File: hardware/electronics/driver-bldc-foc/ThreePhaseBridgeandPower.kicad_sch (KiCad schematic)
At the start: 1 part, among them U1 DRV8353RS

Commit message: fix pcb 20.7.1635
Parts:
- removed U1: DRV8353RS, symbol Custom:DRV8353RS
- added L1: L_Ferrite_Small, Inductor_SMD:L_Cenker_CKCS8040, symbol Device:L_Ferrite_Small
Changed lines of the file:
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@@
 	(paper "A4")
 	(symbol
-		(lib_id "Custom:DRV8353RS")
-		(at 101.6 90.17 0)
+		(lib_id "Device:L_Ferrite_Small")
+		(at 35.56 35.56 0)
 		(unit 1)
 		(body_style 1)
@@
 		(dnp no)
 		(fields_autoplaced yes)
-		(property "Reference" "U1"
-			(at 101.6 44.45 0)
+		(property "Reference" "L1"
+			(at 38.1 34.2899 0)
 			(show_name no)
 			(do_not_autoplace no)
@@
 					(size 1.27 1.27)
 				)
+				(justify left)
 			)
 		)
-		(property "Value" "DRV8353RS"
-			(at 101.6 46.99 0)
+		(property "Value" "L_Ferrite_Small"
+			(at 38.1 36.8299 0)
 			(show_name no)
 			(do_not_autoplace no)
@@
 					(size 1.27 1.27)
 				)
+				(justify left)
 			)
 		)
-		(property "Footprint" ""
-			(at 21.59 44.45 0)
+		(property "Footprint" "Inductor_SMD:L_Cenker_CKCS8040"
+			(at 35.56 35.56 0)
 			(hide yes)
 			(show_name no)
@@
 		)
 		(property "Datasheet" ""
-			(at 21.59 44.45 0)
+			(at 35.56 35.56 0)
 			(hide yes)
 			(show_name no)
@@
 			)
 		)
-		(property "Description" ""
-			(at 101.6 90.17 0)
+		(property "Description" "Inductor with ferrite core, small symbol"
+			(at 35.56 35.56 0)
 			(hide yes)
 			(show_name no)
@@
 			)
 		)
-		(pin "44"
-		)
-		(pin "27"
-		)
-		(pin "9"
-		)
-		(pin "7"
-		)
-		(pin "32"
-		)
-		(pin "33"
-		)
-		(pin "45"
-		)
-		(pin "30"
-		)
-		(pin "31"
-		)
-		(pin "35"
-		)
-		(pin "29"
-		)
-		(pin "14"
-		)
-		(pin "21"
-		)
-		(pin "16"
-		)
-		(pin "34"
-		)
-		(pin "36"
-		)
-		(pin "49"
-		)
-		(pin "13"
-		)
-		(pin "26"
-		)
-		(pin "47"
-		)
-		(pin "46"
-		)
-		(pin "8"
-		)
-		(pin "28"
-		)
-		(pin "10"
-		)
-		(pin "12"
-		)
-		(pin "23"
-		)
-		(pin "48"
-		)
-		(pin "15"
-		)
-		(pin "22"
-		)
-		(pin "3"
-		)
-		(pin "38"
-		)
-		(pin "37"
-		)
-		(pin "41"
-		)
-		(pin "6"
-		)
-		(pin "17"
-		)
-		(pin "5"
-		)
-		(pin "24"
+		(pin "1"
 		)
 		(pin "2"
-		)
-		(pin "42"
-		)
-		(pin "1"
-		)
-		(pin "20"
-		)
-		(pin "43"
-		)
-		(pin "4"
-		)
-		(pin "11"
-		)
-		(pin "40"
-		)
-		(pin "19"
-		)
-		(pin "25"
-		)
-		(pin "18"
-		)
-		(pin "39"
 		)
 		(instances
 			(project "driver-bldc-foc"
 				(path "/90e88ac4-5a7b-4c35-8236-7462b7e2d3a9/be7198b5-813b-4ab8-b125-bdbfdab5672a"
-					(reference "U1")
+					(reference "L1")
 					(unit 1)
 				)

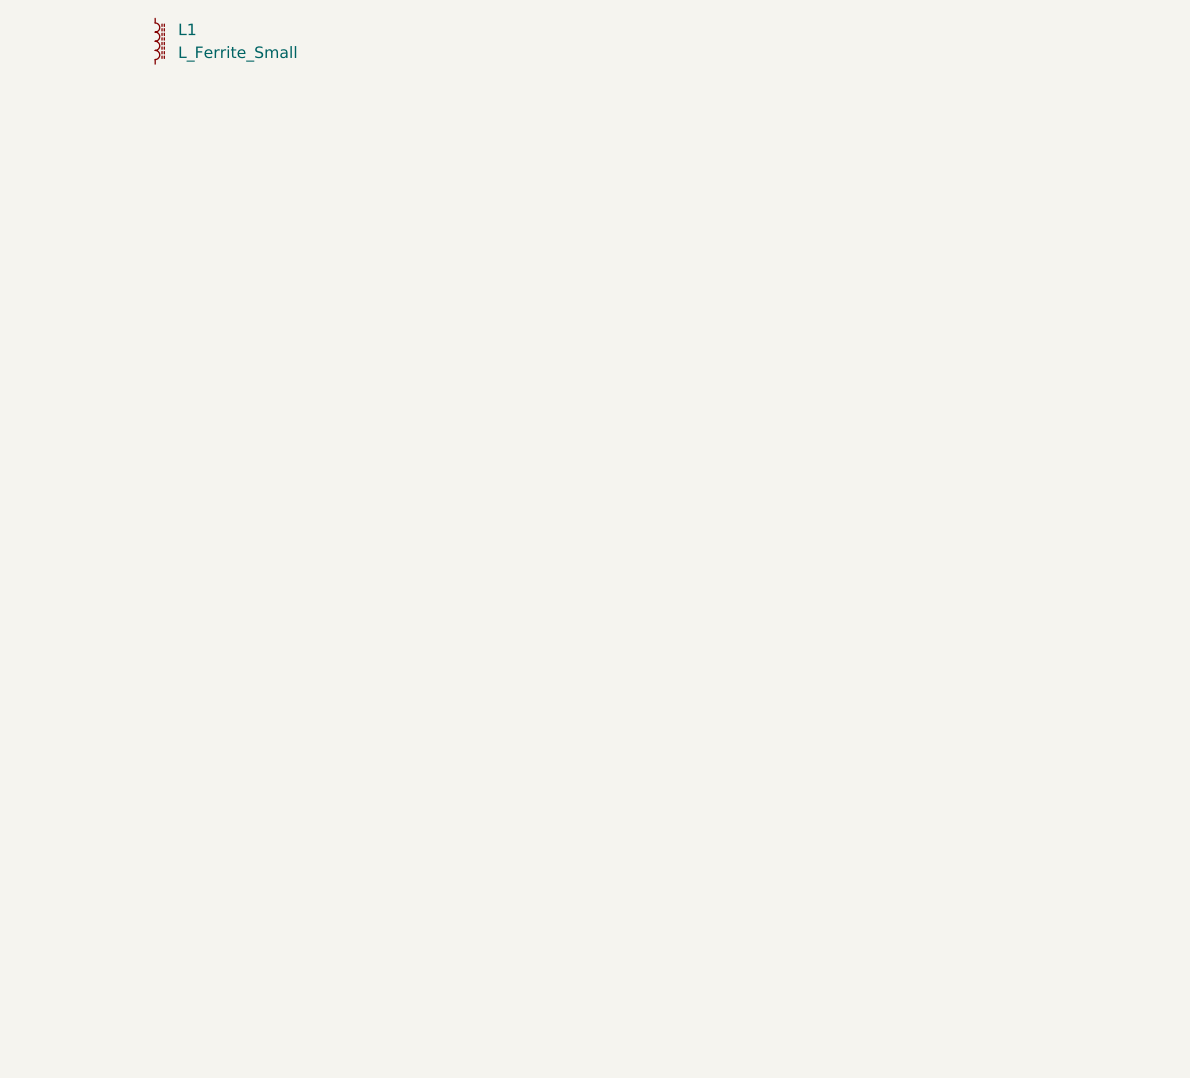
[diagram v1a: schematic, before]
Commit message: update power schematics
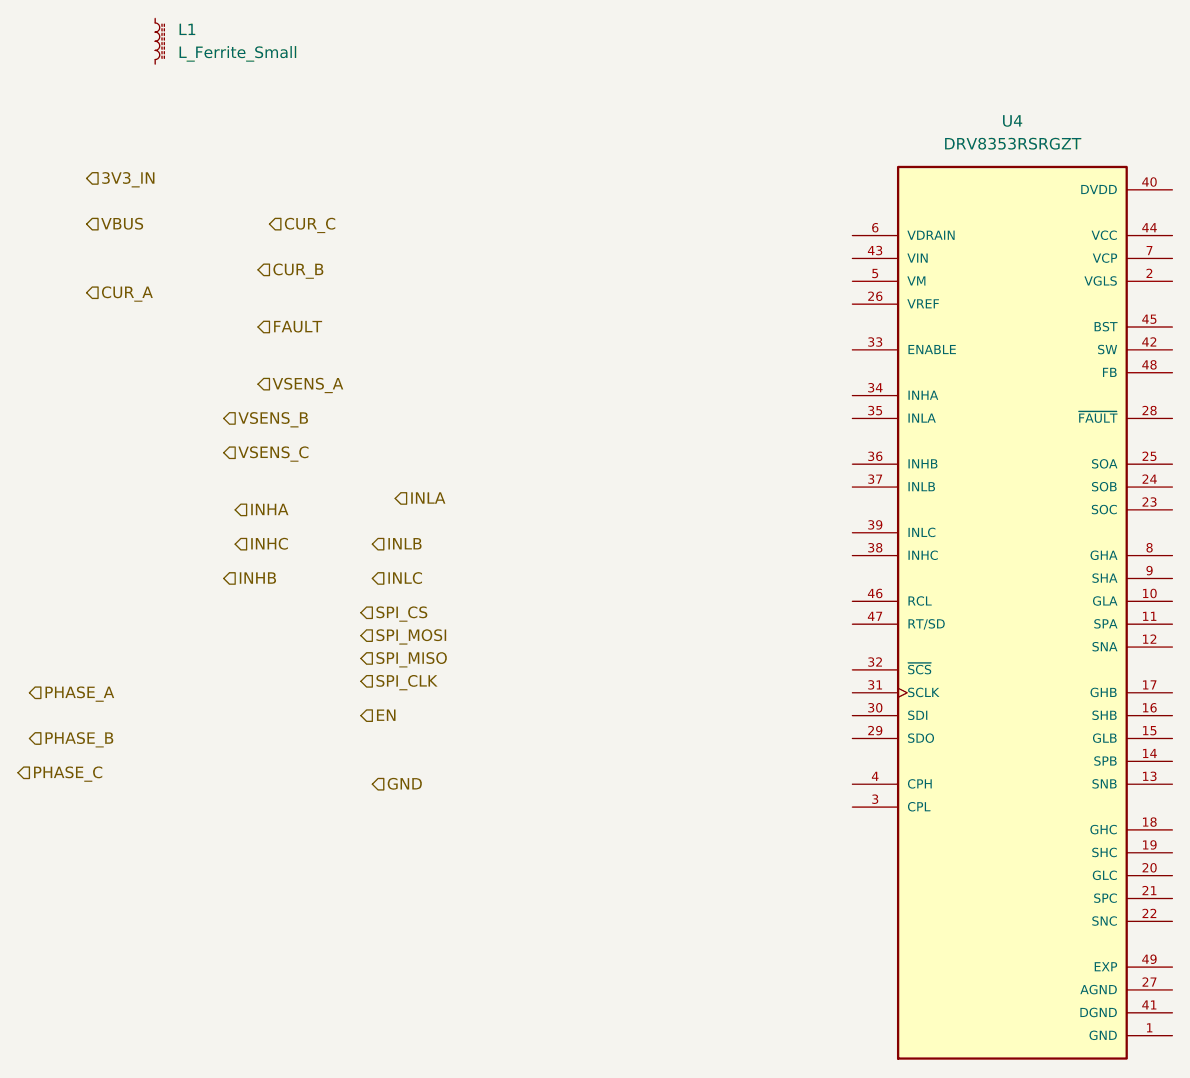
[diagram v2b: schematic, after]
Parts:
- added U4: DRV8353RSRGZT, DRV8353RSRGZT:QFN50P700X700X100-49N, symbol DRV8353RSRGZT:DRV8353RSRGZT

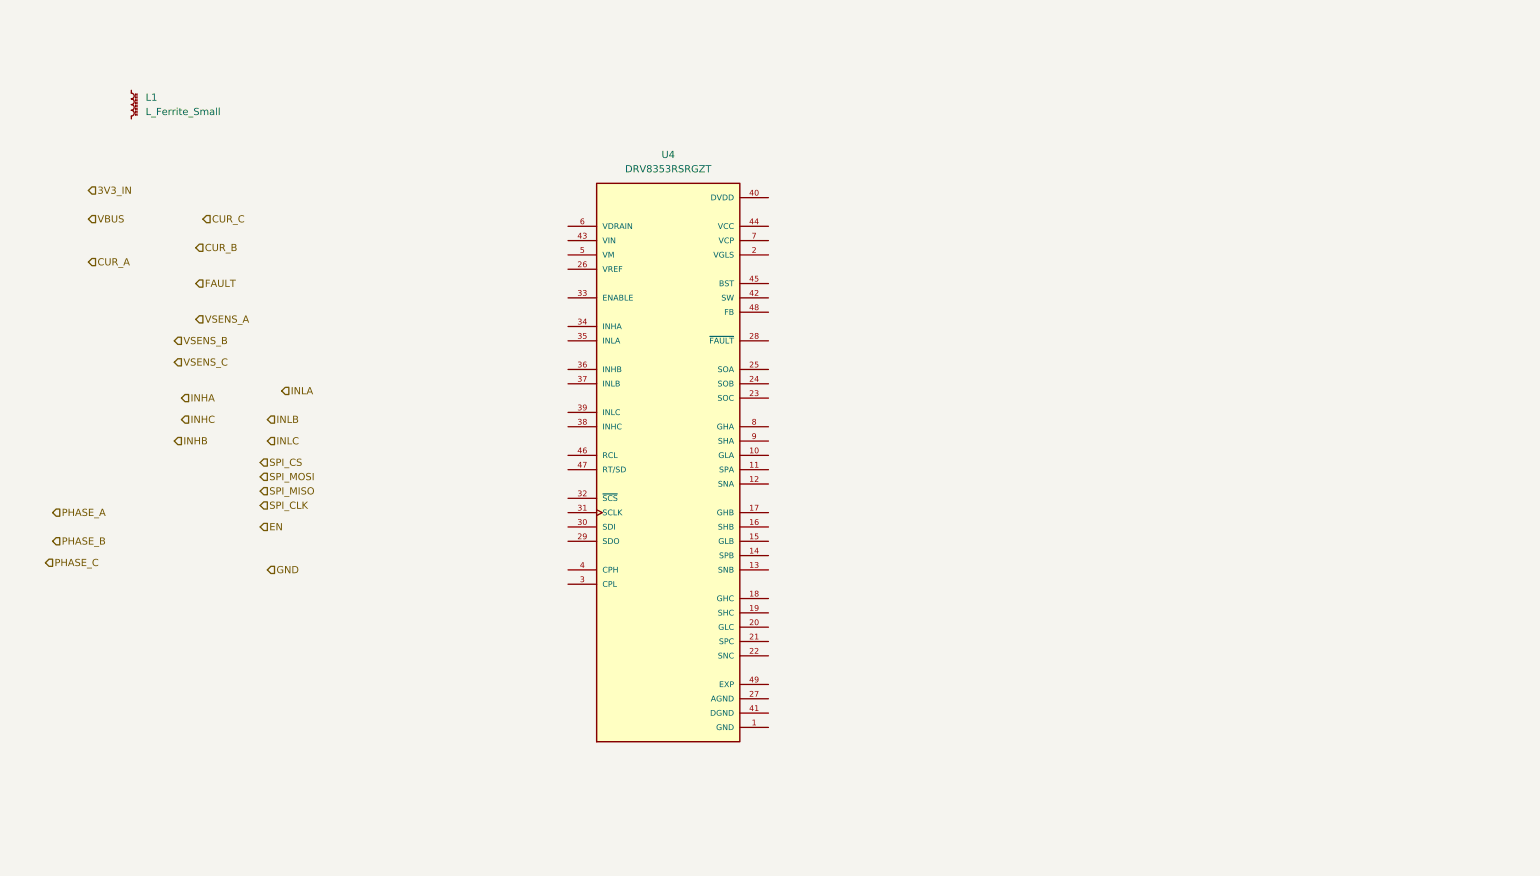
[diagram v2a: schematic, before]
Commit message: update power schematic
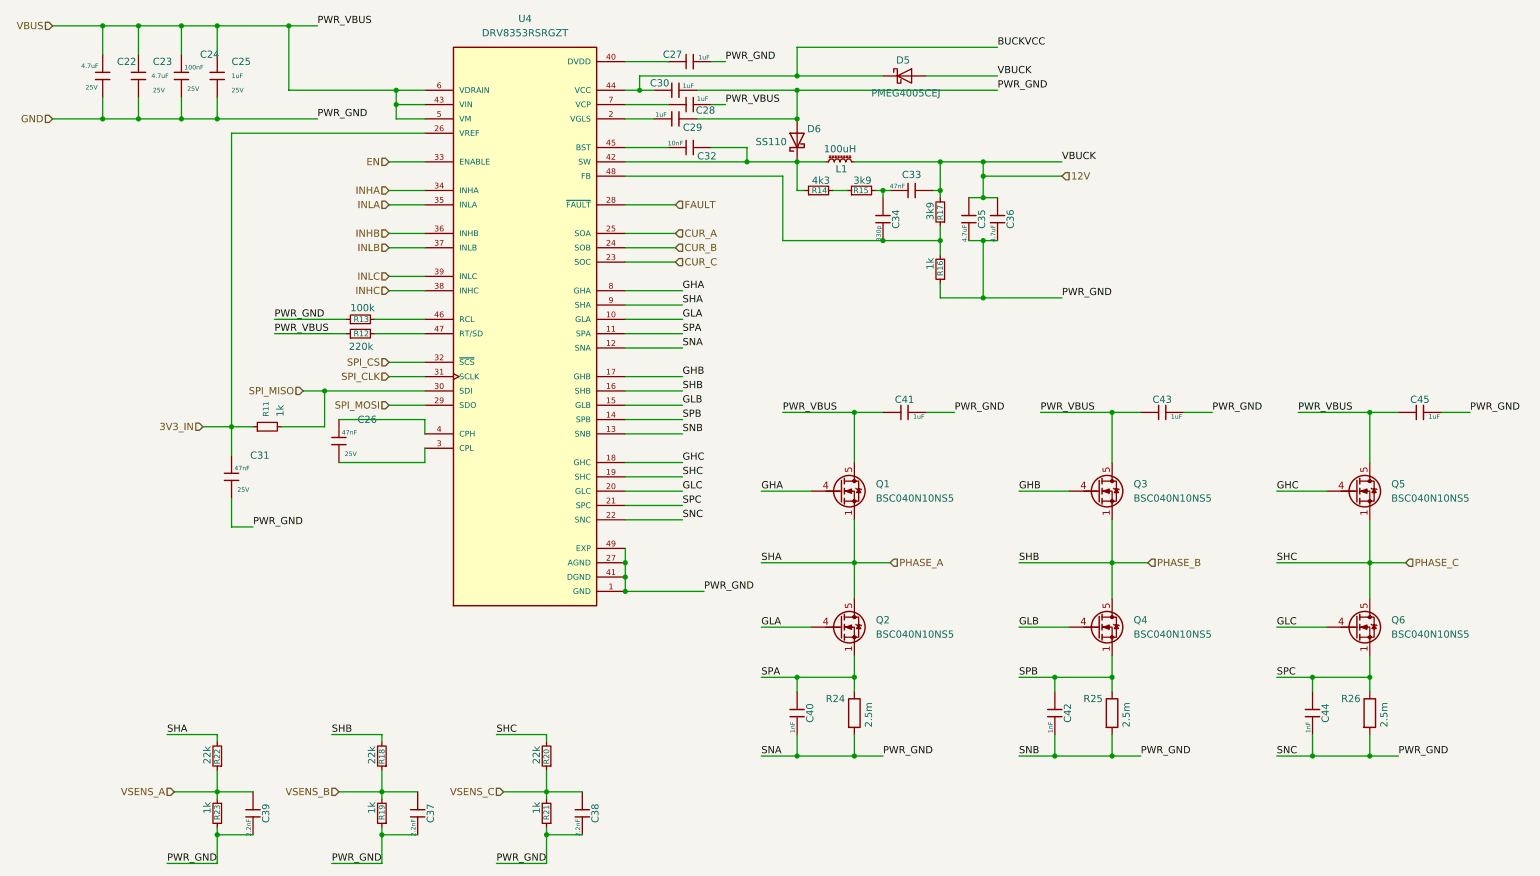
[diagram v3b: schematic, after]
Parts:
- added C22, C23, C35, C36: 4.7uF, Capacitor_SMD:C_0805_2012Metric, symbol JLCPCB-Capacitors:0805,10uF
- added C24: 100nF, Capacitor_SMD:C_0805_2012Metric, symbol JLCPCB-Capacitors:0805,10uF
- added C25, C27, C28, C29, C30, C41, C43, C45: 1uF, Capacitor_SMD:C_0805_2012Metric, symbol JLCPCB-Capacitors:0805,10uF
- added C26, C31, C33: 47nF, Capacitor_SMD:C_0805_2012Metric, symbol JLCPCB-Capacitors:0805,10uF
- added C32: 10nF, Capacitor_SMD:C_0805_2012Metric, symbol JLCPCB-Capacitors:0805,10uF
- added C34: 330p, Capacitor_SMD:C_0805_2012Metric, symbol JLCPCB-Capacitors:0805,10uF
- added C37, C38, C39: 2.2nF, Capacitor_SMD:C_0805_2012Metric, symbol JLCPCB-Capacitors:0805,10uF
- added C40, C42, C44: 1nF, Capacitor_SMD:C_0805_2012Metric, symbol JLCPCB-Capacitors:0805,10uF
- added D5: PMEG4005CEJ, Diode_SMD:D_SOD-323F, symbol Diode:PMEG4005CEJ
- added D6: SS110, Diode_SMD:D_SMA, symbol Diode:SS110
- added Q1, Q2, Q3, Q4, Q5, Q6: BSC040N10NS5, Package_TO_SOT_SMD:TDSON-8-1, symbol Transistor_FET:BSC040N10NS5
- added R11, R16, R19, R21, R23: 1k, Resistor_SMD:R_0805_2012Metric, symbol Device:R_Small
- added R12: 220k, Resistor_SMD:R_0805_2012Metric, symbol Device:R_Small
- added R13: 100k, Resistor_SMD:R_0805_2012Metric, symbol Device:R_Small
- added R14: 4k3, Resistor_SMD:R_0805_2012Metric, symbol Device:R_Small
- added R15, R17: 3k9, Resistor_SMD:R_0805_2012Metric, symbol Device:R_Small
- added R18, R20, R22: 22k, Resistor_SMD:R_0805_2012Metric, symbol Device:R_Small
- added R24, R25, R26: 2.5m, Resistor_SMD:R_2512_6332Metric, symbol Device:R
- L1: value L_Ferrite_Small -> 100uH
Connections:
- net 3V3_IN: now also U4.26 (VREF), C31.1, R11.1
- net CUR_A: now also U4.25 (SOA)
- net CUR_B: now also U4.24 (SOB)
- net CUR_C: now also U4.23 (SOC)
- net EN: now also U4.33 (ENABLE)
- net FAULT: now also U4.28 (~{FAULT})
- net GND: now also U4.1 (GND), U4.12 (SNA), U4.13 (SNB), U4.22 (SNC), U4.27 (AGND), U4.41 (DGND), U4.49 (EXP), C22.2, C23.2, C24.2, C25.2, C27.2, C29.2, C30.2, C31.2, C35.1, C36.1, C37.1, C38.1, C39.1, C40.1, C41.1, C42.1, C43.1, C44.1, C45.1, D6.2 (A), R13.1, R16.1, R19.1, R21.1, R23.1, R24.2, R25.2, R26.2
- net INHA: now also U4.34 (INHA)
- net INHB: now also U4.36 (INHB)
- net INHC: now also U4.38 (INHC)
- net INLA: now also U4.35 (INLA)
- net INLB: now also U4.37 (INLB)
- net INLC: now also U4.39 (INLC)
- net PHASE_A: now also U4.9 (SHA), Q1.1 (S), Q1.2 (S), Q1.3 (S), Q2.5 (D), R22.2
- net PHASE_B: now also U4.16 (SHB), Q3.1 (S), Q3.2 (S), Q3.3 (S), Q4.5 (D), R18.2
- net PHASE_C: now also U4.19 (SHC), Q5.1 (S), Q5.2 (S), Q5.3 (S), Q6.5 (D), R20.2
- net SPI_CLK: now also U4.31 (SCLK)
- net SPI_CS: now also U4.32 (~{SCS})
- net SPI_MISO: now also U4.30 (SDI), R11.2
- net SPI_MOSI: now also U4.29 (SDO)
- net VBUS: now also U4.43 (VIN), U4.5 (VM), U4.6 (VDRAIN), C22.1, C23.1, C24.1, C25.1, C28.2, C41.2, C43.2, C45.2, Q1.5 (D), Q3.5 (D), Q5.5 (D), R12.1
- net VSENS_A: now also C39.2, R22.1, R23.2
- net VSENS_B: now also C37.2, R18.1, R19.2
- net VSENS_C: now also C38.2, R20.1, R21.2
- net GLA: now reaches U4.10 (GLA)
- net GLA: now also Q2.4 (G)
- net SPA: now reaches U4.11 (SPA)
- net SPA: now also C40.2, Q2.1 (S), Q2.2 (S), Q2.3 (S), R24.1
- net SPB: now reaches U4.14 (SPB)
- net SPB: now also C42.2, Q4.1 (S), Q4.2 (S), Q4.3 (S), R25.1
- net GLB: now reaches U4.15 (GLB)
- net GLB: now also Q4.4 (G)
- net GHB: now reaches U4.17 (GHB)
- net GHB: now also Q3.4 (G)
- net GHC: now reaches U4.18 (GHC)
- net GHC: now also Q5.4 (G)
- net at U4.2 (VGLS): now also C29.1
- net GLC: now reaches U4.20 (GLC)
- net GLC: now also Q6.4 (G)
- net SPC: now reaches U4.21 (SPC)
- net SPC: now also C44.2, Q6.1 (S), Q6.2 (S), Q6.3 (S), R26.1
- net at U4.3 (CPL): now also C26.2
- net at U4.4 (CPH): now also C26.1
- net at U4.40 (DVDD): now also C27.1
- net at U4.42 (SW): now also L1.1, C32.2, D6.1 (K), R14.1
- net BUCKVCC: now reaches U4.44 (VCC)
- net BUCKVCC: now also C30.1, D5.1 (K)
- net at U4.45 (BST): now also C32.1
- net at U4.46 (RCL): now also R13.2
- net at U4.47 (RT/SD): now also R12.2
- net at U4.48 (FB): now also C34.1, R16.2, R17.1
- net at U4.7 (VCP): now also C28.1
- net GHA: now reaches U4.8 (GHA)
- net GHA: now also Q1.4 (G)
- net 12V: now reaches L1.2
- net 12V: now also C33.2, C35.2, C36.2, D5.2 (A), R17.2
- new net: R14.2, R15.1
- new net: C33.1, C34.2, R15.2
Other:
- moved on the sheet: L1, U4

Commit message: modify power schematic
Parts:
- C22, C23, C25: footprint Capacitor_SMD:C_0805_2012Metric -> Capacitor_SMD:C_1210_3225Metric
- C41, C43, C45: footprint Capacitor_SMD:C_0805_2012Metric -> Capacitor_SMD:C_1206_3216Metric
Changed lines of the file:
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@@
 			)
 		)
-		(property "Footprint" "Capacitor_SMD:C_0805_2012Metric"
+		(property "Footprint" "Capacitor_SMD:C_1210_3225Metric"
 			(at 28.702 30.48 90)
 			(hide yes)
@@
 			)
 		)
-		(property "Footprint" "Capacitor_SMD:C_0805_2012Metric"
+		(property "Footprint" "Capacitor_SMD:C_1206_3216Metric"
 			(at 218.44 88.392 90)
 			(hide yes)
@@
 			)
 		)
-		(property "Footprint" "Capacitor_SMD:C_0805_2012Metric"
+		(property "Footprint" "Capacitor_SMD:C_1210_3225Metric"
 			(at 35.052 30.48 90)
 			(hide yes)
@@
 			)
 		)
-		(property "Footprint" "Capacitor_SMD:C_0805_2012Metric"
+		(property "Footprint" "Capacitor_SMD:C_1206_3216Metric"
 			(at 172.72 88.392 90)
 			(hide yes)
@@
 			)
 		)
-		(property "Footprint" "Capacitor_SMD:C_0805_2012Metric"
+		(property "Footprint" "Capacitor_SMD:C_1206_3216Metric"
 			(at 264.16 88.392 90)
 			(hide yes)
@@
 			)
 		)
-		(property "Footprint" "Capacitor_SMD:C_0805_2012Metric"
+		(property "Footprint" "Capacitor_SMD:C_1210_3225Metric"
 			(at 49.022 30.48 90)
 			(hide yes)

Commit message: Update driver-bldc-foc schematics, PCB layout, and DRC reports
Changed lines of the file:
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@@
 	)
 	(junction
+		(at 125.73 27.94)
+		(diameter 0)
+		(color 0 0 0 0)
+	)
+	(junction
 		(at 179.07 50.8)
 		(diameter 0)
@@
 	(wire
 		(pts
+			(xy 125.73 25.4) (xy 125.73 27.94)
+		)
+		(stroke
+			(width 0)
+			(type default)
+		)
+	)
+	(wire
+		(pts
 			(xy 168.91 59.69) (xy 179.07 59.69)
 		)
@@
 	(wire
 		(pts
-			(xy 123.19 27.94) (xy 130.81 27.94)
+			(xy 123.19 27.94) (xy 125.73 27.94)
 		)
 		(stroke
@@
 	(wire
 		(pts
+			(xy 125.73 27.94) (xy 130.81 27.94)
+		)
+		(stroke
+			(width 0)
+			(type default)
+		)
+	)
+	(wire
+		(pts
 			(xy 238.76 137.16) (xy 245.11 137.16)
 		)
@@
 					(unit 1)
 				)
+			)
+		)
+	)
+	(symbol
+		(lib_id "power:PWR_FLAG")
+		(at 125.73 25.4 0)
+		(unit 1)
+		(body_style 1)
+		(exclude_from_sim no)
+		(in_bom yes)
+		(on_board yes)
+		(in_pos_files yes)
+		(dnp no)
+		(fields_autoplaced yes)
+		(property "Reference" "#FLG08"
+			(at 125.73 23.495 0)
+			(hide yes)
+			(show_name no)
+			(do_not_autoplace no)
+			(effects
+				(font
+					(size 1.27 1.27)
+				)
+			)
+		)
+		(property "Value" "PWR_FLAG"
+			(at 125.73 20.32 0)
+			(show_name no)
+			(do_not_autoplace no)
+			(effects
+				(font
+					(size 1.27 1.27)
+				)
+			)
+		)
+		(property "Footprint" ""
+			(at 125.73 25.4 0)
+			(hide yes)
+			(show_name no)
+			(do_not_autoplace no)
+			(effects
+				(font
+					(size 1.27 1.27)
+				)
+			)
+		)
+		(property "Datasheet" ""
+			(at 125.73 25.4 0)
+			(hide yes)
+			(show_name no)
+			(do_not_autoplace no)
+			(effects
+				(font
+					(size 1.27 1.27)
+				)
+			)
+		)
+		(property "Description" "Special symbol for telling ERC where power comes from"
+			(at 125.73 25.4 0)
+			(hide yes)
+			(show_name no)
+			(do_not_autoplace no)
+			(effects
+				(font
+					(size 1.27 1.27)
+				)
+			)
+		)
+		(pin "1"
+		)
+		(instances
+			(project "driver-bldc-foc"
+				(path "/90e88ac4-5a7b-4c35-8236-7462b7e2d3a9/be7198b5-813b-4ab8-b125-bdbfdab5672a"
+					(reference "#FLG08")
+					(unit 1)
+				)
